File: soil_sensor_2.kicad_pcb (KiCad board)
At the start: 2 copper layers, 26 x 150 mm, 29 parts, among them J1 ESP-PROG, Q1 SI2312, U1 SHT40, U2 TPS61201DRCT, U3 ESP32-PICO-V3

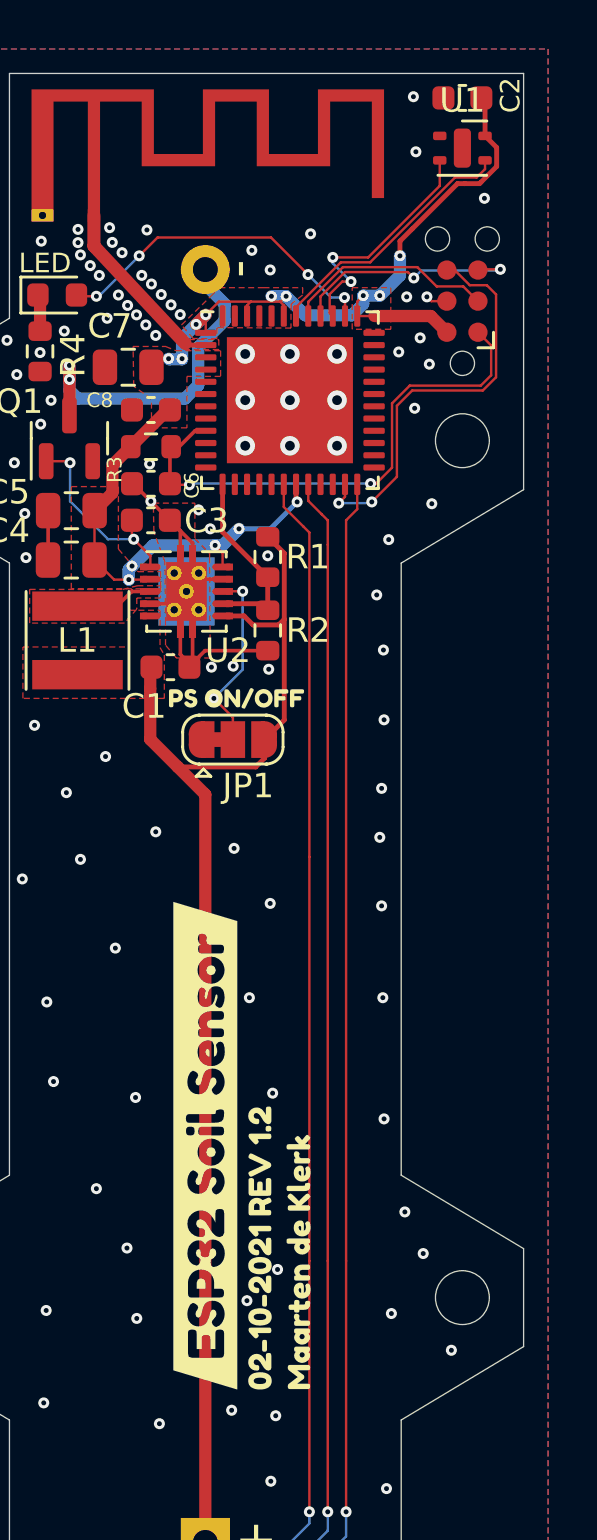
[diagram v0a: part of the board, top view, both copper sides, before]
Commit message: update board version label
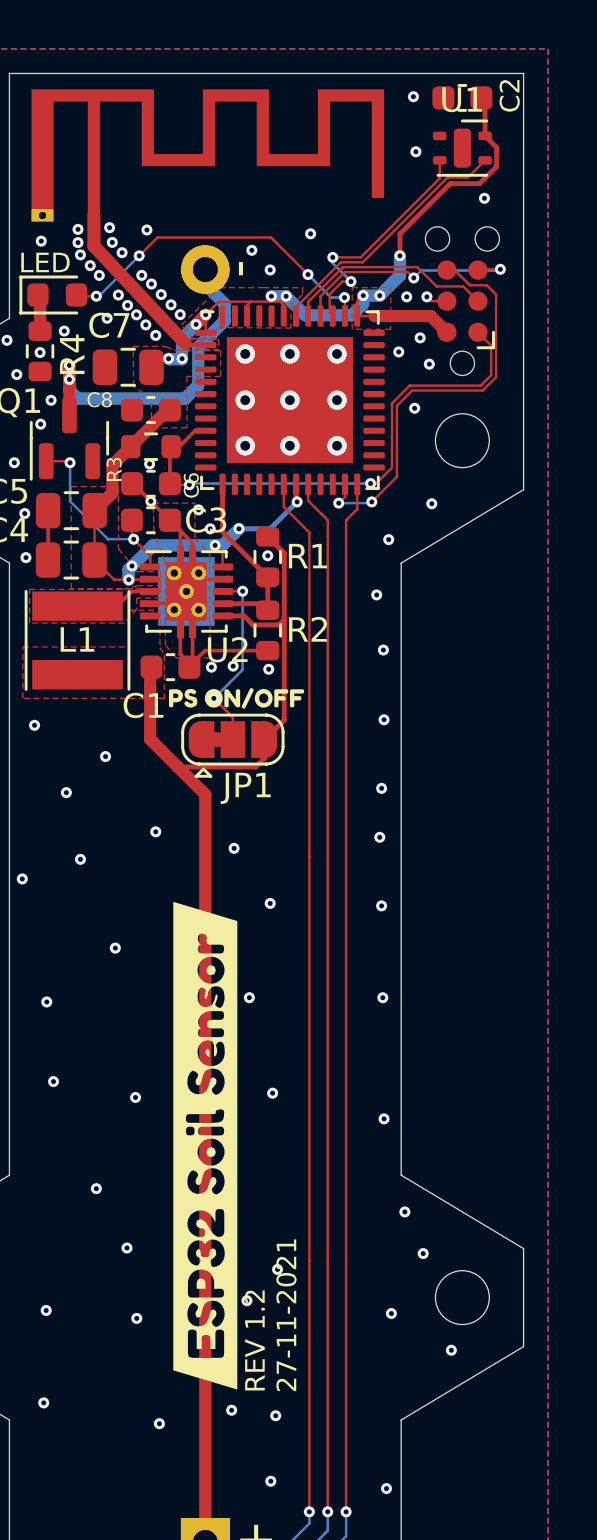
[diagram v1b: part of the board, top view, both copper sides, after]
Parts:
- removed kibuzzard-61586EDB: G***, kibuzzard-61586EDB
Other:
- board text added: "REV 1.2 27-11-2021"

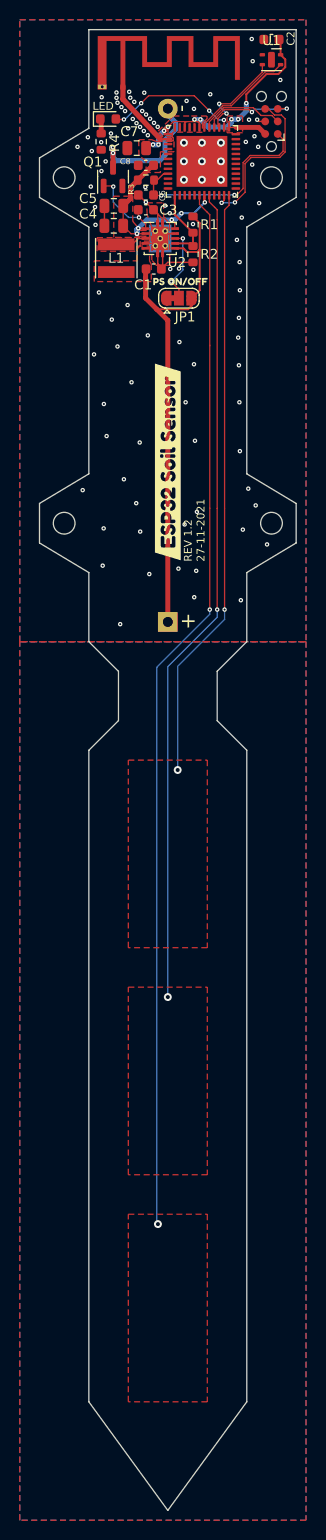
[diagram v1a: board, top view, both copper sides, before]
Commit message: move battery off pcb
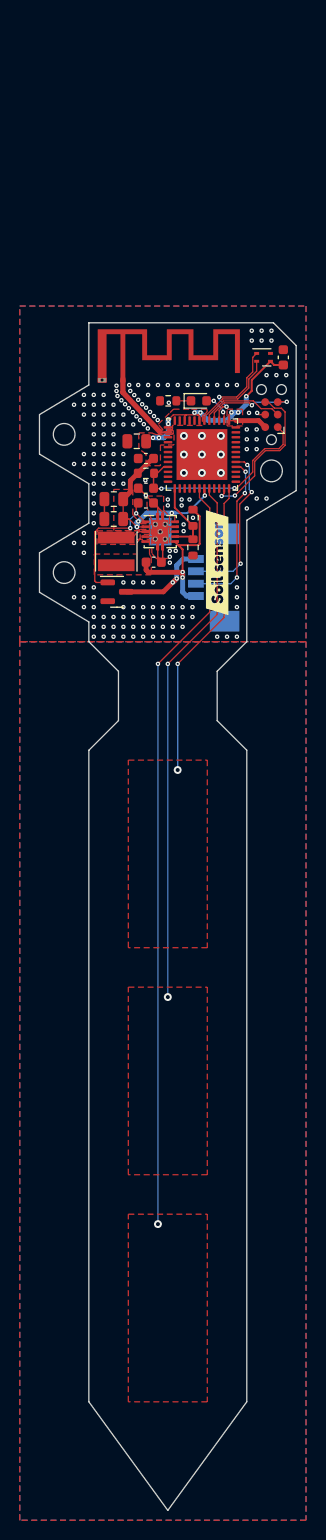
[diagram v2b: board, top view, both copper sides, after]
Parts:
- removed BT1: LiFePo4, Soil_Sensor:BatteryHolder_Keystone_2460_1xAA
- removed JP1: SolderJumper_3_Bridged12, Jumper:SolderJumper-3_P1.3mm_Bridged12_RoundedPad1.0x1.5mm
- removed the REF** at (114.5, 105.0)
- removed kibuzzard-61439F56: G***, kibuzzard-61439F56
- removed kibuzzard-61586E44: G***, kibuzzard-61586E44
- added J1: 532610471, Soil_Sensor:MOLEX_532610471, B.Cu at (109.2, 110.5)
- added kibuzzard-61BE000A: G***, kibuzzard-61BE000A, B.Cu at (103.8, 111.1)
- added kibuzzard-61BE0016: G***, kibuzzard-61BE0016, B.Cu at (103.8, 112.4)
- added kibuzzard-61BE001F: G***, kibuzzard-61BE001F, B.Cu at (103.8, 109.9)
- added kibuzzard-61BE0025: G***, kibuzzard-61BE0025, B.Cu at (103.8, 108.6)
- added kibuzzard-61BE0345: G***, kibuzzard-61BE0345, F.Cu at (109.0, 109.0)
- R1: value 2M -> 1M5
- U1: value SHT40 -> SHT4x; footprint Sensor_Humidity:Sensirion_DFN-4-1EP_2x2mm_P1mm_EP0.7x1.6mm -> Soil_Sensor:XDCR_SHT40-AD1B-R2
- moved Q1 42.1 mm to (98.8, 112.0), turned to 0 degrees
- moved C1 32.2 mm to (115.7, 88.2), turned to 90 degrees
- moved U1 30.2 mm to (113.7, 88.2)
- moved D1 30.0 mm to (107.1, 92.6)
- moved AE1 29.7 mm to (99.5, 90.5)
- moved C2 29.7 mm to (102.6, 109.0)
- moved C3 29.7 mm to (101.8, 103.0)
- moved C4 29.7 mm to (98.5, 104.6)
- moved C6 29.7 mm to (101.8, 101.5)
- moved C7 29.7 mm to (100.8, 96.7)
- moved J2 29.7 mm to (114.5, 94.0)
- moved L1 29.7 mm to (98.8, 107.9)
- moved R1 29.7 mm to (106.5, 104.5)
- moved R2 29.7 mm to (106.5, 107.5)
- moved REF** 29.7 mm to (114.5, 99.7)
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- renumbered C2 to C1, C1 to C2, J1 to J2
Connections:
- U1 pad 1: GND -> /SDA_{0}
- U1 pad 2: /SCL -> /SCL_{0}
- U1 pad 3: /SDA -> +3V3
- U1 pad 4: +3V3 -> GND
- U2 pad 8: Net-(JP1-Pad2) -> GND
- U3 pad 28: unconnected-(U3-Pad28) -> /SDA_{1}
- U3 pad 29: unconnected-(U3-Pad29) -> /SCL_{1}
- U3 pad 39: /SCL -> /SDA_{0}
- U3 pad 42: /SDA -> /SCL_{0}
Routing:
- net /BAT+: track 52.8 -> 18.1 mm, vias 0 -> 2
- net /CAP_SENSE_3: track 106.9 -> 77.1 mm
- net /CAP_SENSE_2: track 83.6 -> 53.9 mm
- net /CAP_SENSE_1: track 60.3 -> 30.7 mm
- net /SCL_{1}: track 0.00 -> 16.9 mm, vias 0 -> 3
- net /SDA_{1}: track 0.00 -> 16.7 mm, vias 0 -> 3
- net Net-(D1-Pad2): track 13.7 -> 3.17 mm, vias 4 -> 2
- net /SDA: track 10.6 -> 0.00 mm
- net /SDA_{0}: track 0.00 -> 10.2 mm, vias 0 -> 2
- net /SCL: track 9.76 -> 0.00 mm, vias 2 -> 0
- net /SCL_{0}: track 0.00 -> 9.11 mm
- net Net-(JP1-Pad2): track 7.40 -> 0.00 mm, vias 2 -> 0
- net Net-(C3-Pad1): track 8.04 -> 14.3 mm
- net /BAT-: track 14.2 -> 9.78 mm
- net GND: track 16.9 -> 13.5 mm, vias 102 -> 182
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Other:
- board size 26 x 150 mm -> 26 x 120.3 mm
- board text added: "REV 1.3 09-12-2021"
- board text removed: "+"
- board text removed: "-"
- board text removed: "LED"
- board text removed: "REV 1.2 27-11-2021"
